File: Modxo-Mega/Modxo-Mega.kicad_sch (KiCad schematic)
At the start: 4 parts, among them J8 DBG

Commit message: Cleanup schematic
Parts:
- renumbered J8 to J9
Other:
- sheet MCU ports: added D0, DBG_NRST, DBG_SWCLK, DBG_SWDIO, EXP_SCL, EXP_SDA, LCD_CSN1, LCD_CSN2, LCD_SPI_SCK, LCD_SPI_TX, RGB_DOUT, UART_RX, UART_TX, XSMBUS_SCL, XSMBUS_SDA; removed none
- note removed: "Connectors"
- note removed: "Debug"
- moved on the sheet: FID1, FID2, FID3, J9

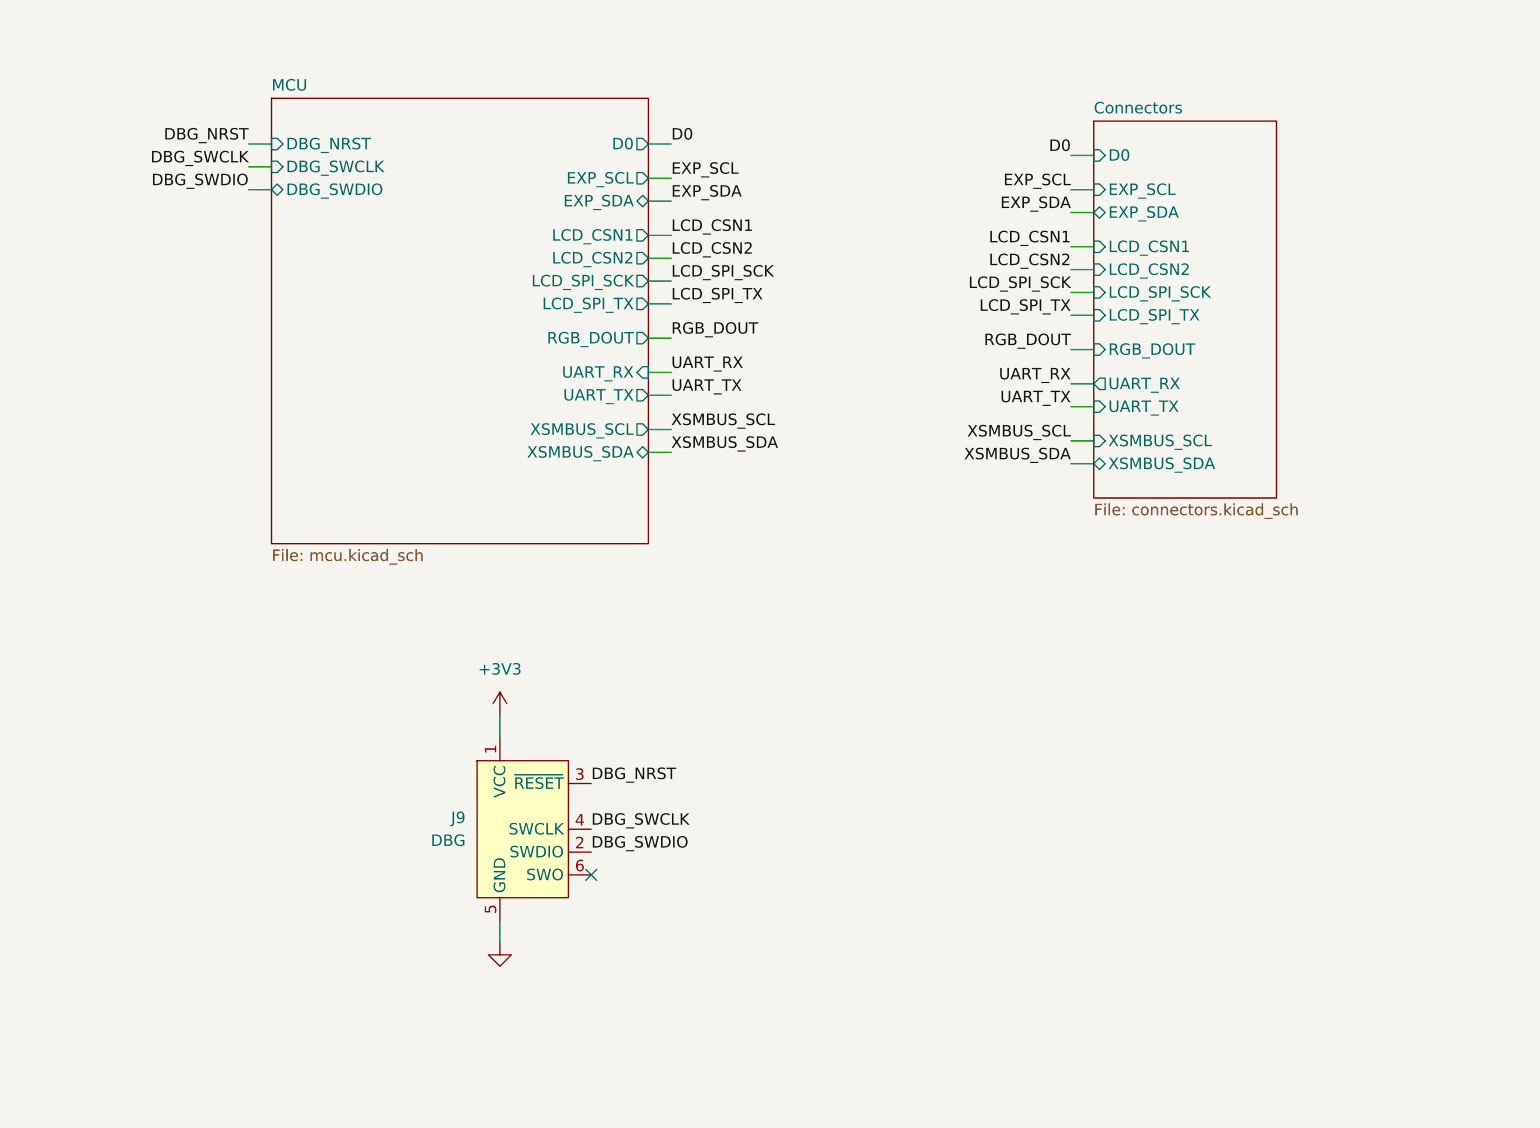
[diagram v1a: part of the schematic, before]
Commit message: Add SD Card, other minor changes
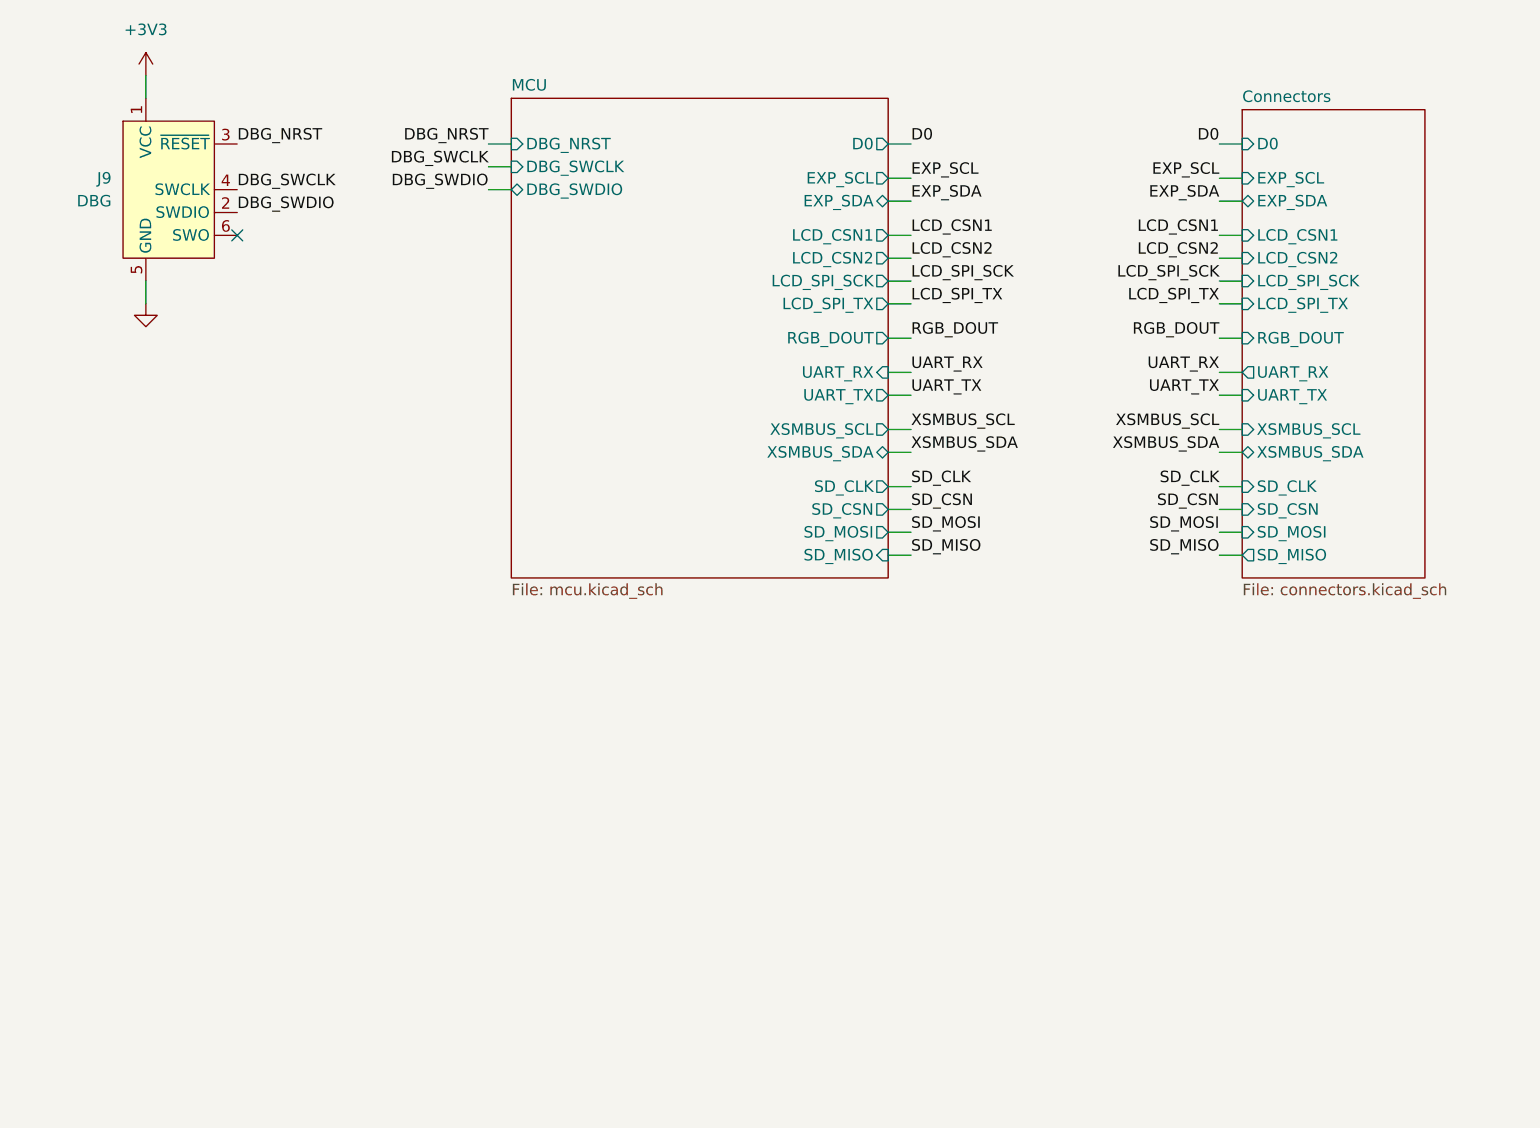
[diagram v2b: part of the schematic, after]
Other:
- sheet Connectors ports: added SD_CLK, SD_CSN, SD_MISO, SD_MOSI; removed none
- sheet MCU ports: added SD_CLK, SD_CSN, SD_MISO, SD_MOSI; removed none
- moved on the sheet: J9
